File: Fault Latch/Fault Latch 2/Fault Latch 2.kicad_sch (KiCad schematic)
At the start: 80 parts, among them K101 Fujitsu_FTR-LYAA005x, K102 Fujitsu_FTR-LYAA005x, K103 Fujitsu_FTR-LYAA005x, Q104 Q_NPN_BEC, Q106 Q_NPN_BEC, Q107 Q_NPN_BEC, Q108 Q_NPN_BEC, Q109 Q_NMOS_GDS, Q110 Q_NMOS_GDS, Q111 Q_NMOS_GDS, Q112 Q_NPN_BEC, Q113 Q_NPN_BEC, SW101 SW_Omron_B3FS, SW102 SW_Omron_B3FS, SW103 SW_Omron_B3FS, U101 641964-1, U102 74AHC1G00, U103 74AHC1G00, U104 74AHC1G00, U105 641964-1, U106 74LS279, U107 SFH617A-1, U108 SFH617A-1, U109 SFH617A-1, U110 641964-1, U111 641964-1, U112 641964-1, U113 641964-1, U114 SFH617A-1, U115 SFH617A-1, U116 SFH617A-1

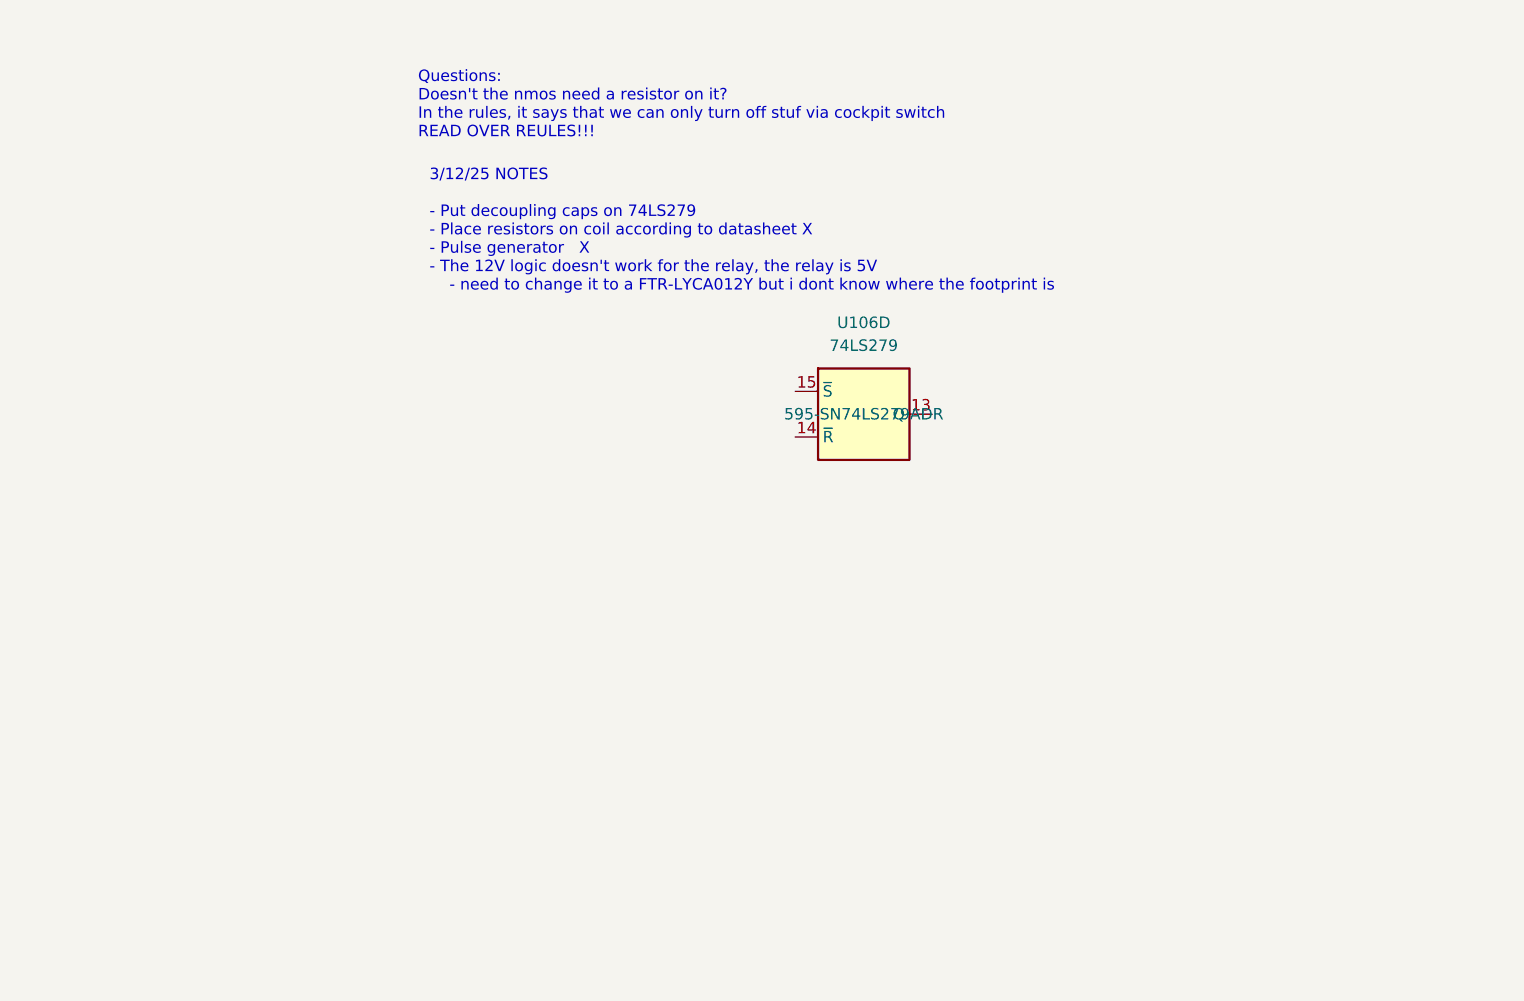
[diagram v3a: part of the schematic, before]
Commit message: showed an error on the fault latch
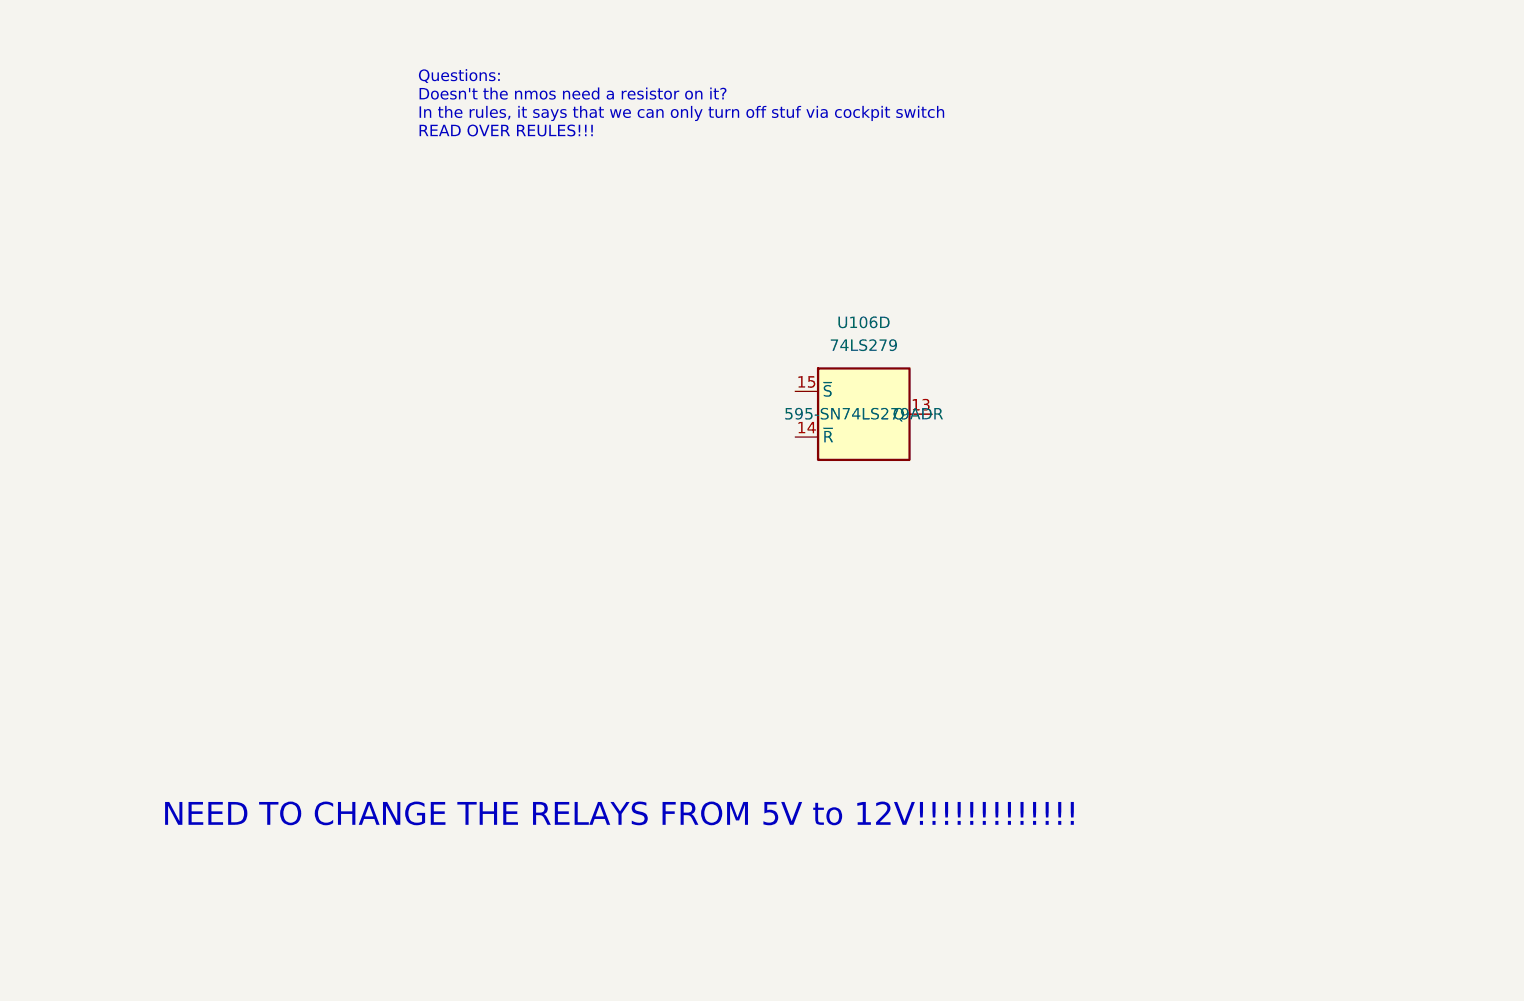
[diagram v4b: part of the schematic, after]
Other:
- note added: "NEED TO CHANGE THE RELAYS FROM 5V to 12V!!!!!!!!!!!!!"
- note removed: "3/12/25 NOTES - Put decoupling caps on 74LS279 - Place resistors on coil according to datasheet X - Pulse generator X - The 12V logic doesn't work for the relay, the relay is 5V - need to change it to a FTR-LYCA012Y but i dont know where the footprint is"
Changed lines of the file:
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@@
 		)
 	)
-	(text "3/12/25 NOTES\n\n- Put decoupling caps on 74LS279\n- Place resistors on coil according to datasheet X\n- Pulse generator   X\n- The 12V logic doesn't work for the relay, the relay is 5V\n	- need to change it to a FTR-LYCA012Y but i dont know where the footprint is\n"
+	(text "NEED TO CHANGE THE RELAYS FROM 5V to 12V!!!!!!!!!!!!!"
 		(exclude_from_sim no)
-		(at 316.23 121.92 0)
+		(at 286.512 186.944 0)
 		(effects
 			(font
-				(size 1.27 1.27)
+				(size 2.54 2.54)
+				(color 255 32 36 1)
 			)
 			(justify left)

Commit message: cleaned up fault latch a little
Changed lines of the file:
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@@
 					(size 1.27 1.27)
 				)
+				(hide yes)
 			)
 		)
@@
 					(size 1.27 1.27)
 				)
+				(hide yes)
 			)
 		)
@@
 					(size 1.27 1.27)
 				)
+				(hide yes)
 			)
 		)
@@
 					(size 1.27 1.27)
 				)
+				(hide yes)
 			)
 		)
@@
 					(size 1.27 1.27)
 				)
+				(hide yes)
 			)
 		)
@@
 					(size 1.27 1.27)
 				)
+				(hide yes)
 			)
 		)
@@
 					(size 1.27 1.27)
 				)
+				(hide yes)
 			)
 		)
@@
 					(size 1.27 1.27)
 				)
+				(hide yes)
 			)
 		)
@@
 					(size 1.27 1.27)
 				)
+				(hide yes)
 			)
 		)
@@
 					(size 1.27 1.27)
 				)
+				(hide yes)
 			)
 		)
@@
 					(size 1.27 1.27)
 				)
+				(hide yes)
 			)
 		)
@@
 					(size 1.27 1.27)
 				)
+				(hide yes)
 			)
 		)
@@
 					(size 1.27 1.27)
 				)
+				(hide yes)
 			)
 		)
@@
 					(size 1.27 1.27)
 				)
+				(hide yes)
 			)
 		)
@@
 					(size 1.27 1.27)
 				)
+				(hide yes)
 			)
 		)
@@
 					(size 1.27 1.27)
 				)
+				(hide yes)
 			)
 		)
@@
 					(size 1.27 1.27)
 				)
+				(hide yes)
 			)
 		)
@@
 					(size 1.27 1.27)
 				)
+				(hide yes)
 			)
 		)
@@
 					(size 1.27 1.27)
 				)
+				(hide yes)
 			)
 		)
@@
 					(size 1.27 1.27)
 				)
+				(hide yes)
 			)
 		)
@@
 					(size 1.27 1.27)
 				)
+				(hide yes)
 			)
 		)
@@
 					(size 1.27 1.27)
 				)
+				(hide yes)
 			)
 		)
@@
 					(size 1.27 1.27)
 				)
+				(hide yes)
 			)
 		)
@@
 					(size 1.27 1.27)
 				)
+				(hide yes)
 			)
 		)
@@
 					(size 1.27 1.27)
 				)
+				(hide yes)
 			)
 		)
@@
 					(size 1.27 1.27)
 				)
+				(hide yes)
 			)
 		)
@@
 					(size 1.27 1.27)
 				)
+				(hide yes)
 			)
 		)
@@
 					(size 1.27 1.27)
 				)
+				(hide yes)
 			)
 		)
@@
 					(size 1.27 1.27)
 				)
+				(hide yes)
 			)
 		)
@@
 					(size 1.27 1.27)
 				)
+				(hide yes)
 			)
 		)
@@
 					(size 1.27 1.27)
 				)
+				(hide yes)
 			)
 		)
@@
 					(size 1.27 1.27)
 				)
+				(hide yes)
 			)
 		)
@@
 					(size 1.27 1.27)
 				)
+				(hide yes)
 			)
 		)
@@
 					(size 1.27 1.27)
 				)
+				(hide yes)
 			)
 		)
@@
 					(size 1.27 1.27)
 				)
+				(hide yes)
 			)
 		)
@@
 					(size 1.27 1.27)
 				)
+				(hide yes)
 			)
 		)
@@
 					(size 1.27 1.27)
 				)
+				(hide yes)
 			)
 		)
@@
 					(size 1.27 1.27)
 				)
+				(hide yes)
 			)
 		)
@@
 					(size 1.27 1.27)
 				)
+				(hide yes)
 			)
 		)
@@
 					(size 1.27 1.27)
 				)
+				(hide yes)
 			)
 		)
@@
 					(size 1.27 1.27)
 				)
+				(hide yes)
 			)
 		)
@@
 					(size 1.27 1.27)
 				)
+				(hide yes)
 			)
 		)
@@
 					(size 1.27 1.27)
 				)
+				(hide yes)
 			)
 		)
@@
 					(size 1.27 1.27)
 				)
+				(hide yes)
 			)
 		)
@@
 					(size 1.27 1.27)
 				)
+				(hide yes)
 			)
 		)
@@
 					(size 1.27 1.27)
 				)
+				(hide yes)
 			)
 		)
@@
 					(size 1.27 1.27)
 				)
+				(hide yes)
 			)
 		)
@@
 					(size 1.27 1.27)
 				)
+				(hide yes)
 			)
 		)
@@
 					(size 1.27 1.27)
 				)
+				(hide yes)
 			)
 		)
@@
 					(size 1.27 1.27)
 				)
+				(hide yes)
 			)
 		)
@@
 					(size 1.27 1.27)
 				)
+				(hide yes)
 			)
 		)
@@
 					(size 1.27 1.27)
 				)
+				(hide yes)
 			)
 		)
@@
 					(size 1.27 1.27)
 				)
+				(hide yes)
 			)
 		)
@@
 					(size 1.27 1.27)
 				)
+				(hide yes)
 			)
 		)
@@
 					(size 1.27 1.27)
 				)
+				(hide yes)
 			)
 		)
@@
 					(size 1.27 1.27)
 				)
+				(hide yes)
 			)
 		)
@@
 					(size 1.27 1.27)
 				)
+				(hide yes)
 			)
 		)
@@
 					(size 1.27 1.27)
 				)
+				(hide yes)
 			)
 		)
@@
 					(size 1.27 1.27)
 				)
+				(hide yes)
 			)
 		)
@@
 					(size 1.27 1.27)
 				)
+				(hide yes)
 			)
 		)
@@
 					(size 1.27 1.27)
 				)
+				(hide yes)
 			)
 		)
@@
 					(size 1.27 1.27)
 				)
+				(hide yes)
 			)
 		)
@@
 					(size 1.27 1.27)
 				)
+				(hide yes)
 			)
 		)
@@
 					(size 1.27 1.27)
 				)
+				(hide yes)
 			)
 		)

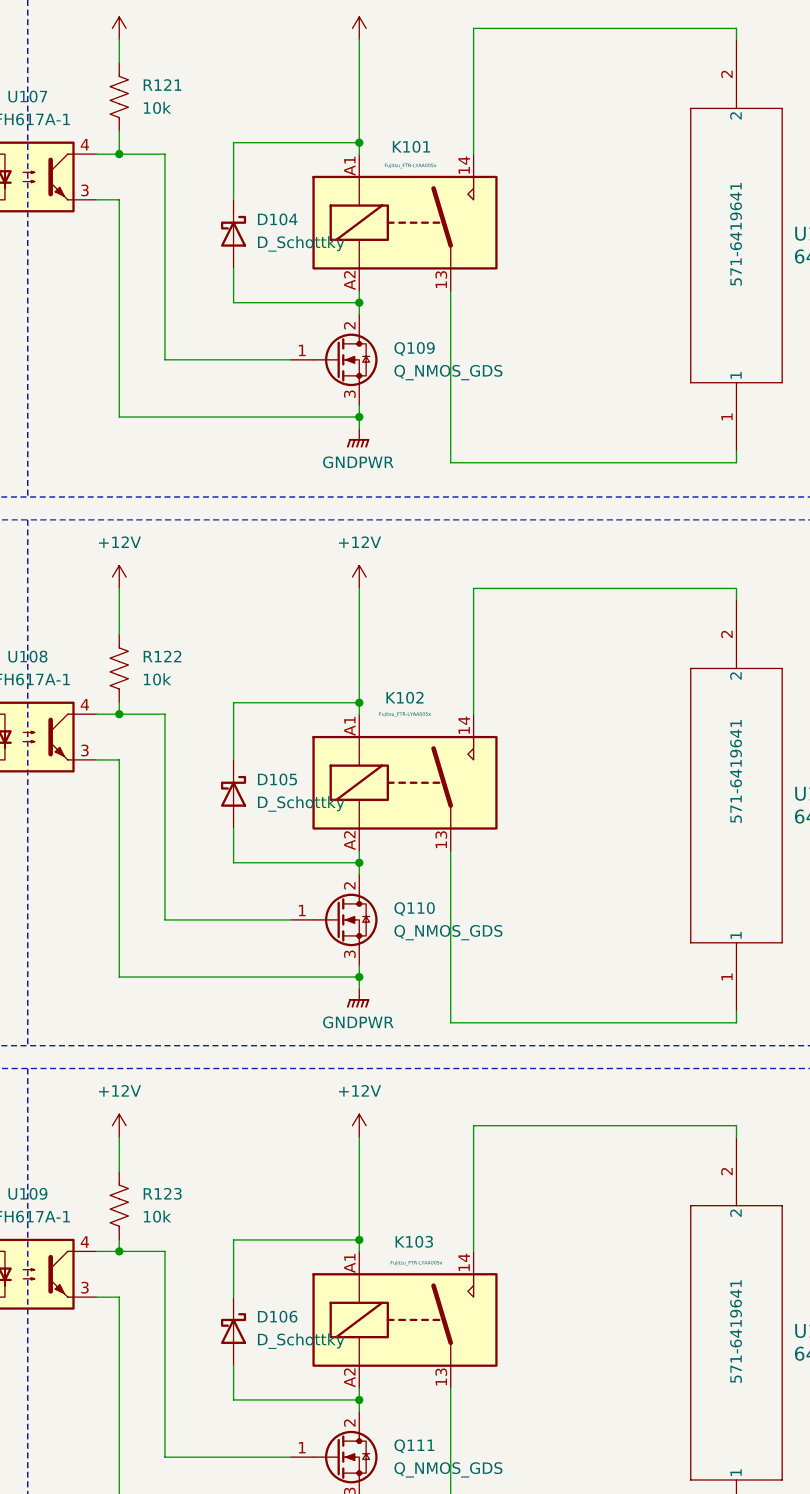
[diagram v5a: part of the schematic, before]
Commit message: minor updates to fault latch and RML pcb layout
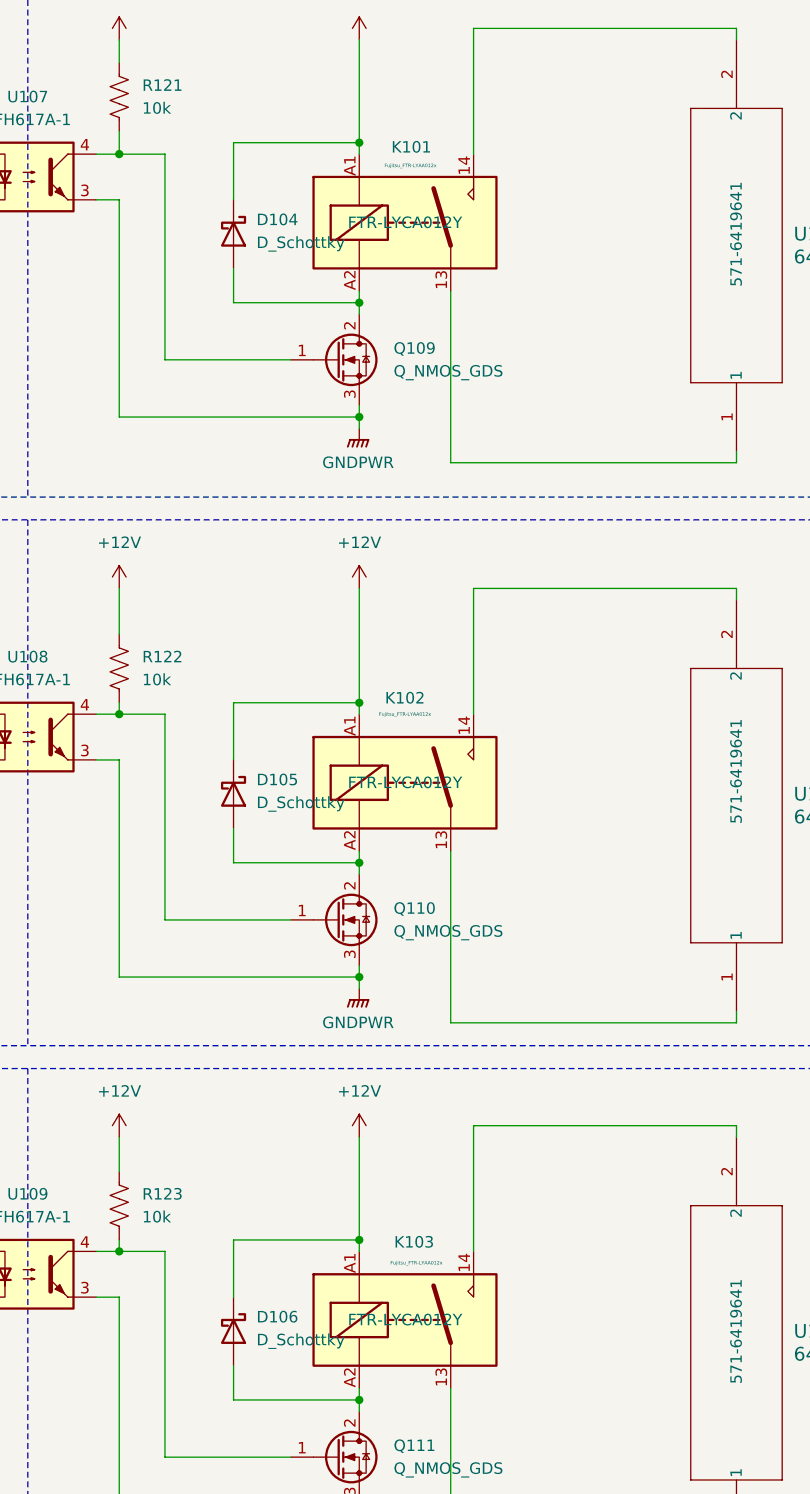
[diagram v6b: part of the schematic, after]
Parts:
- K101, K102, K103: value Fujitsu_FTR-LYAA005x -> Fujitsu_FTR-LYAA012x; JLC# C1222376 -> (none); MOUSER (none) -> FTR-LYCA012Y
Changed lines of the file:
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@@
 			)
 		)
-		(property "Value" "Fujitsu_FTR-LYAA005x"
+		(property "Value" "Fujitsu_FTR-LYAA012x"
 			(at 189.484 153.67 0)
 			(effects
@@
 			)
 		)
-		(property "JLC#" "C1222376"
+		(property "JLC#" " "
 			(at 203.2 161.9249 0)
 			(effects
@@
 			)
 		)
-		(property "MOUSER" ""
+		(property "MOUSER" "FTR-LYCA012Y "
 			(at 191.77 160.02 0)
 			(effects
@@
 			)
 		)
-		(property "Value" "Fujitsu_FTR-LYAA005x"
+		(property "Value" "Fujitsu_FTR-LYAA012x"
 			(at 193.04 275.59 0)
 			(effects
@@
 			)
 		)
-		(property "JLC#" "C1222376"
+		(property "JLC#" " "
 			(at 191.77 285.496 0)
 			(effects
@@
 			)
 		)
-		(property "MOUSER" ""
+		(property "MOUSER" "FTR-LYCA012Y "
 			(at 191.77 281.94 0)
 			(effects
@@
 			)
 		)
-		(property "Value" "Fujitsu_FTR-LYAA005x"
+		(property "Value" "Fujitsu_FTR-LYAA012x"
 			(at 191.77 214.63 0)
 			(effects
@@
 			)
 		)
-		(property "JLC#" "C1222376"
+		(property "JLC#" " "
 			(at 191.77 226.06 0)
 			(effects
@@
 			)
 		)
-		(property "MOUSER" ""
+		(property "MOUSER" "FTR-LYCA012Y "
 			(at 191.77 222.25 0)
 			(effects

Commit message: TSSI has been integrated into fault latch.
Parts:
- removed D101, D102: RED, LED_SMD:LED_0805_2012Metric_Pad1.15x1.40mm_HandSolder, symbol Device:LED
- removed R117, R118: 270R, Resistor_SMD:R_0805_2012Metric_Pad1.20x1.40mm_HandSolder, symbol Device:R_US
- removed R121: 10k, Resistor_SMD:R_0805_2012Metric_Pad1.20x1.40mm_HandSolder, symbol Device:R_US
- removed U107, U108, U109: SFH617A-1, Package_DIP:DIP-4_W7.62mm, symbol Isolator:SFH617A-1
- added C113: 1u, Capacitor_SMD:C_0402_1005Metric, symbol Device:C_Polarized_US
- added C114, C117: 0.1u, Capacitor_SMD:C_0402_1005Metric, symbol Device:C
- added C115: .01u, Capacitor_SMD:C_0402_1005Metric, symbol Device:C
- added C116: 22u, Capacitor_SMD:C_0402_1005Metric, symbol Device:C
- added D1, D2, D3, D4: US2AA, Diode_SMD:D_SMA, symbol Diode:US2AA
- added D107, D108: RED, LED_SMD:LED_0805_2012Metric_Pad1.15x1.40mm_HandSolder, symbol Device:LED
- added Q102, Q115, Q116: Q_NMOS_GSD, Package_TO_SOT_SMD:SOT-23, symbol Transistor_FET:Q_NMOS_GSD
- added Q114, Q117, Q118, Q119: Q_NMOS_GDS, Package_TO_SOT_SMD:TO-252-2, symbol Transistor_FET:Q_NMOS_GDS
- added R111: 15k, Resistor_SMD:R_0603_1608Metric, symbol Device:R_US
- added R130: 100k, Resistor_SMD:R_0603_1608Metric, symbol Device:R_US
- added R132, R143: 10k, Resistor_SMD:R_0603_1608Metric, symbol Device:R_US
- added R133, R134, R136: 270R, Resistor_SMD:R_0805_2012Metric_Pad1.20x1.40mm_HandSolder, symbol Device:R_US
- added R137, R138, R139, R140, R141, R142: 10k, Resistor_SMD:R_0805_2012Metric_Pad1.20x1.40mm_HandSolder, symbol Device:R_US
- added U118: LM555xM, Package_SO:SOIC-8_3.9x4.9mm_P1.27mm, symbol Timer:LM555xM
- added U119, U121, U122: 641964-1, 641964-1:TE_641964-1, symbol CONNECTOR:641964-1
- added U120: 74AHC1G08, Package_TO_SOT_SMD:SOT-353_SC-70-5, symbol 74xGxx:74AHC1G08
- added U123, U125, U126: SFH617A-1, Package_DIP:DIP-4_W7.62mm, symbol Isolator:SFH617A-1
- K101, K103: value Fujitsu_FTR-LYAA012x -> Fujitsu_FTR-LYAA005x; JLC# (none) -> C1222376; MOUSER FTR-LYCA012Y -> (none)
- K102: value Fujitsu_FTR-LYAA012x -> Fujitsu_FTR-LYAA005x; JLC# (none) -> C1222376; MOUSER FTR-LYCA012Y -> (none); Notes (none) -> basically a 157 ohm resistor
- R104, R105, R107: value 270R -> 10k
- R116: value 270R -> 500R; footprint Resistor_SMD:R_0805_2012Metric_Pad1.20x1.40mm_HandSolder -> Resistor_SMD:R_0603_1608Metric; JLC# C17590 -> C130232
- R122: value 10k -> 270R; footprint Resistor_SMD:R_0805_2012Metric_Pad1.20x1.40mm_HandSolder -> Resistor_SMD:R_0603_1608Metric; JLC# C17414 -> C130232
- R123: footprint Resistor_SMD:R_0805_2012Metric_Pad1.20x1.40mm_HandSolder -> Resistor_SMD:R_0603_1608Metric; JLC# C17414 -> C130232
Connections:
- net +12V: now also R116.1, R137.1, R138.1, R139.1, R140.1, R143.1, U121.2; no longer D104.1 (K), D105.1 (K), D106.1 (K), K101.A1, K102.A1, K103.A1, R123.2
- net +5V: now also D106.1 (K), K103.A1, C113.1, C114.1, C117.1, R130.2, R133.2, R134.2, R136.2, R141.1, R142.1, U118.4 (R), U118.8 (VCC), U120.5 (VCC), U123.1, U125.1; no longer R116.2
- net GND: now also Q109.3 (S), Q110.3 (S), Q111.3 (S), C113.2, C114.2, C115.2, C116.1, C117.2, Q102.2 (S), Q118.3 (S), Q119.3 (S), U118.1 (GND), U120.3 (GND), U126.2
- net GNDPWR: now also R123.1, Q114.3 (S), Q115.2 (S), Q116.2 (S), Q117.3 (S), U123.3, U125.3, U126.3; no longer Q109.3 (S), Q110.3 (S), Q111.3 (S)
- net NBMS_LV: now also R107.2; no longer D103.1 (K)
- net NBPSD_LV: now also R105.2
- net NIMD_LV: now also R104.2
- net BMS_SR: now reaches D104.2 (A), K101.A2, Q109.2 (D)
- net BMS_SR: now also Q118.1 (G)
- net IMD_SR: now reaches D105.2 (A), K102.A2, Q110.2 (D)
- net IMD_SR: now also Q119.1 (G)
- net at U106.9 (Q): now also Q111.1 (G), D108.1 (K)
- net at Q109.1 (G): now also D103.1 (K), U106.4 (Q)
- net at D103.2 (A): now also R133.1; no longer R107.2
- net at R122.1: now also U119.2; no longer Q110.1 (G)
- net at U106.7 (Q): now also Q110.1 (G), D107.1 (K)
- new net: D3.1 (K), D4.1 (K), U120.1
- new net: R132.1, U120.4
- new net: D104.1 (K), K101.A1, U123.2
- new net: Q117.1 (G), R138.2, U123.4
- new net: D105.1 (K), K102.A1, U125.2
- new net: D108.2 (A), R136.1
- new net: R132.2, U126.1
- new net: Q115.1 (G), R143.2, U126.4
- new net: Q102.3 (D), U122.1
- new net: R116.2, U122.2
- new net: D3.2 (A), Q118.2 (D), R141.2
- new net: Q116.3 (D), U119.1
- new net: D4.2 (A), Q119.2 (D), R142.2
- new net: Q115.3 (D), U121.1
- new net: C115.1, U118.5 (CV)
- new net: D1.1 (K), D2.1 (K), Q116.1 (G), R123.2
- new net: Q114.1 (G), R137.2, U125.4
- new net BMS_Green: D1.2 (A), Q117.2 (D), R140.2
- new net CLOCK: R111.1, U118.3 (Q), U120.2
- new net IMD_Green: D2.2 (A), Q114.2 (D), R139.2
- new net IMD_LED: D107.2 (A), Q102.1 (G), R134.1
- new net THRESH: C116.2, R111.2, R130.1, U118.2 (TR), U118.6 (THR)
- no-connect marks 1 -> 2
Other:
- note added: "Was a LED but got replaced --->"
- note added: "f = 1 / (0.693 * (2R106) * C102)"
- note added: "https://www.electronics-tutorials.ws/waveforms/555_oscillator.html"
- note removed: "NEED TO CHANGE THE RELAYS FROM 5V to 12V!!!!!!!!!!!!!"
- moved on the sheet: C103, C104, D103, D104, D106, K101, K103, Q109, Q111, R104, R105, R131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
